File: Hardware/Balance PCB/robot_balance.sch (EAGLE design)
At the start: 58 parts, among them P1 10118194-0001LF, Q1 16Mhz

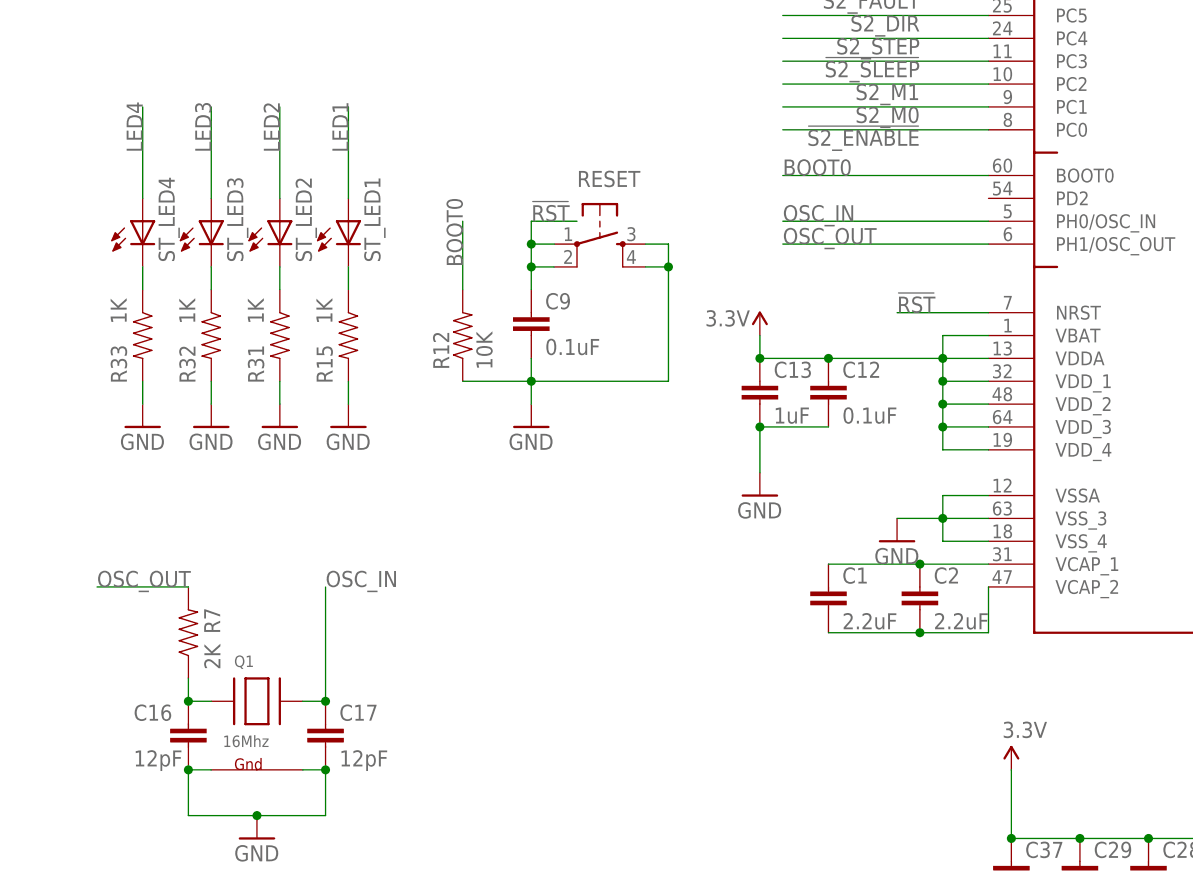
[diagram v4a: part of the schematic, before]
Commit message: Fixed bug with Vcap
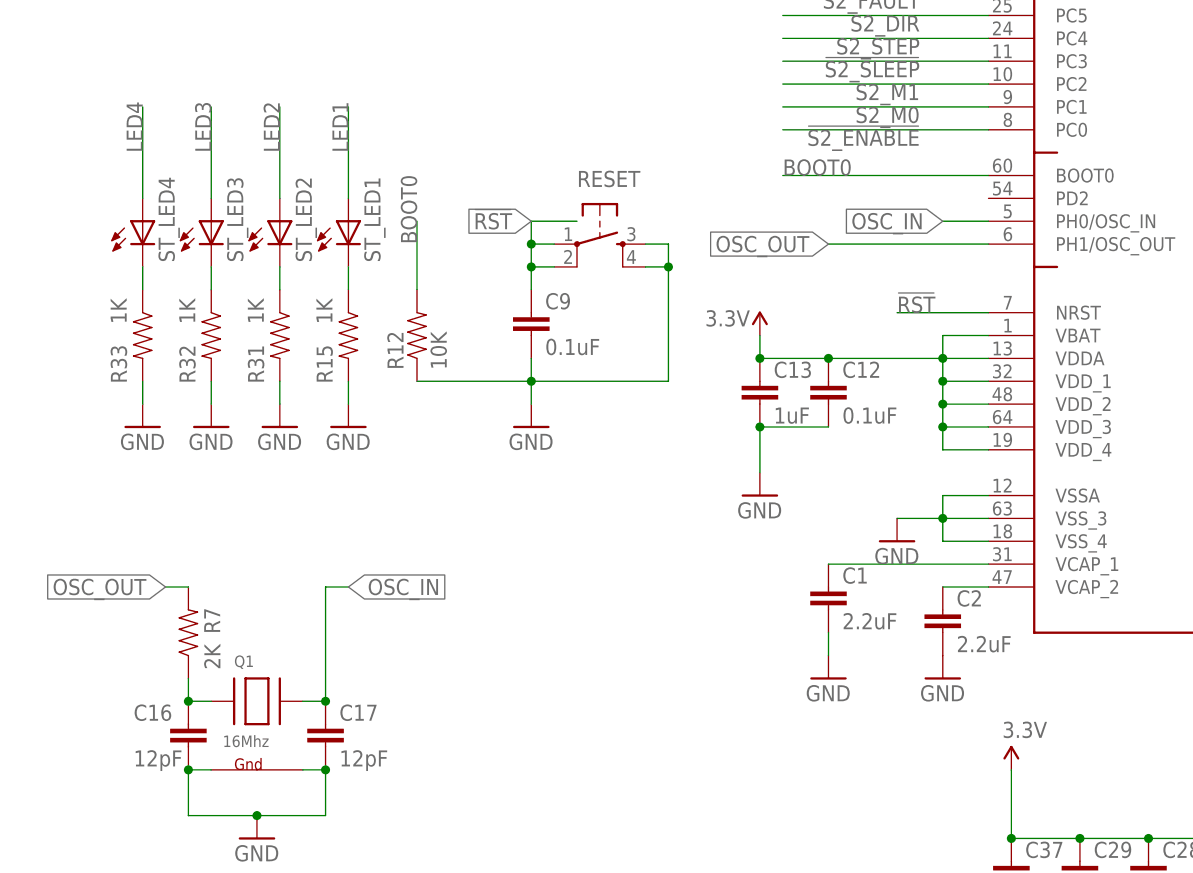
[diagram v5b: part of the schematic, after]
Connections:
- net GND: now also C1.2, C2.2
- net N$12: now also C2.1; no longer C1.2, C2.2
- net N$2: no longer C2.1
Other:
- moved on the sheet: C2, R12
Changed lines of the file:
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@@
 <part name="SUPPLY2" library="SparkFun-Aesthetics" deviceset="5V" device=""/>
 <part name="SUPPLY3" library="SparkFun-Aesthetics" deviceset="5V" device=""/>
+<part name="GND16" library="SparkFun-Aesthetics" deviceset="GND" device=""/>
+<part name="GND17" library="SparkFun-Aesthetics" deviceset="GND" device=""/>
 </parts>
 <sheets>
@@
 <instance part="C38" gate="G$1" x="322.58" y="-160.02"/>
 <instance part="C1" gate="G$1" x="48.26" y="-88.9"/>
-<instance part="C2" gate="G$1" x="58.42" y="-88.9"/>
+<instance part="C2" gate="G$1" x="60.96" y="-91.44"/>
 <instance part="SUPPLY1" gate="G$1" x="68.58" y="-106.68"/>
 <instance part="RESET" gate="S" x="22.86" y="-48.26"/>
 <instance part="C9" gate="G$1" x="15.24" y="-58.42"/>
 <instance part="GND8" gate="1" x="15.24" y="-68.58"/>
-<instance part="R12" gate="G$1" x="7.62" y="-58.42" rot="R90"/>
+<instance part="R12" gate="G$1" x="2.54" y="-58.42" rot="R90"/>
 <instance part="GND21" gate="1" x="40.64" y="-76.2"/>
 <instance part="C12" gate="G$1" x="48.26" y="-66.04"/>
@@
 <instance part="SUPPLY2" gate="G$1" x="312.42" y="2.54"/>
 <instance part="SUPPLY3" gate="G$1" x="312.42" y="55.88"/>
+<instance part="GND16" gate="1" x="48.26" y="-96.52"/>
+<instance part="GND17" gate="1" x="60.96" y="-96.52"/>
 </instances>
 <busses>
@@
 <junction x="15.24" y="-63.5"/>
 <pinref part="R12" gate="G$1" pin="1"/>
-<wire x1="7.62" y1="-63.5" x2="15.24" y2="-63.5" width="0.1524" layer="91"/>
+<wire x1="2.54" y1="-63.5" x2="15.24" y2="-63.5" width="0.1524" layer="91"/>
 <junction x="30.48" y="-50.8"/>
 </segment>
@@
 <junction x="175.26" y="-48.26"/>
 <junction x="190.5" y="-35.56"/>
+</segment>
+<segment>
+<pinref part="C1" gate="G$1" pin="2"/>
+<pinref part="GND16" gate="1" pin="GND"/>
+<wire x1="48.26" y1="-93.98" x2="48.26" y2="-91.44" width="0.1524" layer="91"/>
+</segment>
+<segment>
+<pinref part="C2" gate="G$1" pin="2"/>
+<pinref part="GND17" gate="1" pin="GND"/>
 </segment>
 </net>
@@
 <wire x1="15.24" y1="-48.26" x2="15.24" y2="-45.72" width="0.1524" layer="91"/>
 <wire x1="15.24" y1="-45.72" x2="20.32" y2="-45.72" width="0.1524" layer="91"/>
-<label x="15.24" y="-45.72" size="1.778" layer="95"/>
+<label x="15.24" y="-45.72" size="1.778" layer="95" rot="R180" xref="yes"/>
 </segment>
 <segment>
@@
 <wire x1="-10.16" y1="-99.06" x2="-7.62" y2="-99.06" width="0.1524" layer="91"/>
 <wire x1="-7.62" y1="-99.06" x2="-7.62" y2="-86.36" width="0.1524" layer="91"/>
+<wire x1="-7.62" y1="-86.36" x2="-5.08" y2="-86.36" width="0.1524" layer="91"/>
 <pinref part="C17" gate="G$1" pin="1"/>
 <junction x="-7.62" y="-99.06"/>
 <pinref part="Q1" gate="G$1" pin="X2"/>
-<label x="-7.62" y="-86.36" size="1.778" layer="95"/>
+<label x="-5.08" y="-86.36" size="1.778" layer="95" xref="yes"/>
 </segment>
 <segment>
 <pinref part="U$4" gate="G$1" pin="PH0/OSC_IN"/>
-<wire x1="66.04" y1="-45.72" x2="43.18" y2="-45.72" width="0.1524" layer="91"/>
-<label x="43.18" y="-45.72" size="1.778" layer="95"/>
+<wire x1="66.04" y1="-45.72" x2="60.96" y2="-45.72" width="0.1524" layer="91"/>
+<label x="60.96" y="-45.72" size="1.778" layer="95" rot="R180" xref="yes"/>
 </segment>
 </net>
 <net name="OSC_OUT" class="0">
 <segment>
-<wire x1="-33.02" y1="-86.36" x2="-22.86" y2="-86.36" width="0.1524" layer="91"/>
+<wire x1="-25.4" y1="-86.36" x2="-22.86" y2="-86.36" width="0.1524" layer="91"/>
 <pinref part="R7" gate="G$1" pin="2"/>
-<label x="-33.02" y="-86.36" size="1.778" layer="95"/>
+<label x="-25.4" y="-86.36" size="1.778" layer="95" rot="R180" xref="yes"/>
 </segment>
 <segment>
 <pinref part="U$4" gate="G$1" pin="PH1/OSC_OUT"/>
-<wire x1="66.04" y1="-48.26" x2="43.18" y2="-48.26" width="0.1524" layer="91"/>
-<label x="43.18" y="-48.26" size="1.778" layer="95"/>
+<wire x1="66.04" y1="-48.26" x2="48.26" y2="-48.26" width="0.1524" layer="91"/>
+<label x="48.26" y="-48.26" size="1.778" layer="95" rot="R180" xref="yes"/>
 </segment>
 </net>
@@
 </segment>
 </net>
-<net name="N$2" class="0">
-<segment>
+<net name="N$12" class="0">
+<segment>
+<pinref part="U$4" gate="G$1" pin="VCAP_2"/>
+<wire x1="66.04" y1="-86.36" x2="60.96" y2="-86.36" width="0.1524" layer="91"/>
 <pinref part="C2" gate="G$1" pin="1"/>
-<pinref part="C1" gate="G$1" pin="1"/>
-<wire x1="58.42" y1="-83.82" x2="48.26" y2="-83.82" width="0.1524" layer="91"/>
-<pinref part="U$4" gate="G$1" pin="VCAP_1"/>
-<wire x1="58.42" y1="-83.82" x2="66.04" y2="-83.82" width="0.1524" layer="91"/>
-<junction x="58.42" y="-83.82"/>
-</segment>
-</net>
-<net name="N$12" class="0">
-<segment>
-<pinref part="C1" gate="G$1" pin="2"/>
-<pinref part="C2" gate="G$1" pin="2"/>
-<wire x1="48.26" y1="-91.44" x2="58.42" y2="-91.44" width="0.1524" layer="91"/>
-<pinref part="U$4" gate="G$1" pin="VCAP_2"/>
-<wire x1="66.04" y1="-86.36" x2="66.04" y2="-91.44" width="0.1524" layer="91"/>
-<wire x1="66.04" y1="-91.44" x2="58.42" y2="-91.44" width="0.1524" layer="91"/>
-<junction x="58.42" y="-91.44"/>
 </segment>
 </net>
@@
 <segment>
 <pinref part="R12" gate="G$1" pin="2"/>
-<wire x1="7.62" y1="-53.34" x2="7.62" y2="-45.72" width="0.1524" layer="91"/>
-<label x="7.62" y="-50.8" size="1.778" layer="95" rot="R90"/>
+<wire x1="2.54" y1="-53.34" x2="2.54" y2="-45.72" width="0.1524" layer="91"/>
+<label x="2.54" y="-48.26" size="1.778" layer="95" rot="R90"/>
 </segment>
 </net>
@@
 </segment>
 </net>
+<net name="N$2" class="0">
+<segment>
+<pinref part="U$4" gate="G$1" pin="VCAP_1"/>
+<pinref part="C1" gate="G$1" pin="1"/>
+<wire x1="48.26" y1="-83.82" x2="66.04" y2="-83.82" width="0.1524" layer="91"/>
+</segment>
+</net>
